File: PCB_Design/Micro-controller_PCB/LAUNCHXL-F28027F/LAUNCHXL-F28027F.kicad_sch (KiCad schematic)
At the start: 9 parts, among them CON1 USB_B_Mini, U4 TLV1117-33

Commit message: Finished Page 1 of Micro controller schematic page
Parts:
- added C10, C11: 4u7, symbol Device:C
- added C12, C13, C14, C16: 100n, symbol Device:C
- added C15: 3u3, symbol Device:C
- added C17, C18: 36p, symbol Device:C
- added D7, D8: BLUE, symbol Device:LED
- added JP1, JP2, JP3: Jumper_2_Open, symbol Jumper:Jumper_2_Open
- added L1, L2: 600 Ohm, symbol Device:FerriteBead
- added R16, R18, R19, R20, R21, R25, R28, R30, R32: 0, symbol Device:R
- added R22, R23: 1k, symbol Device:R
- added R24: 12k, symbol Device:R
- added R26, R27: 330, symbol Device:R
- added R29: 10k, symbol Device:R
- added R31: 2k2, symbol Device:R
- added U5: ISO7240MDWRG4, symbol Custom_library:ISO7240MDWRG4
- added U7: ISO7231ADW, symbol Custom_library:ISO7231ADW
- added U8: 93LC56AT-I_OT, symbol Custom_library:93LC56AT-I_OT
- added Y3: ECS-120-18-33-JEM-TR3, symbol Custom_library:ECS-120-18-33-JEM-TR3
- C9: value 0.1u -> 100n
- gave numbers to parts that had none: 1
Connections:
- net D+: now also U6.8 (DP)
- net D-: now also U6.7 (DM)
- net FTDI_3V3: now also U6.20 (VCCIO), U6.31 (VCCIO), U6.42 (VCCIO), U6.50 (VREGIN), U6.56 (VCCIO), C16.1, D7.2 (A), D8.2 (A), JP1.1 (A), L1.2, L2.2, R21.1, R22.2, R29.1, U5.1 (VCC1), U7.16 (VCC2), U8.6 (VCC)
- net GNDA: now also U6.1 (GND), U6.10 (AGND), U6.11 (GND), U6.13 (TEST), U6.15 (GND), U6.25 (GND), U6.35 (GND), U6.47 (GND), U6.5 (GND), U6.51 (GND), U6.65 (GND), C12.2, C13.2, C14.2, C15.2, C16.2, C17.2, C18.2, JP2.1 (A), R23.1, R24.2, R25.1, U5.2 (GND1_1), U5.8 (GND1_2), U7.10 (EN2), U7.15 (GND2_2), U7.9 (GND2_1), U8.2 (GND), Y3.2 (GND_1), Y3.4 (GND_2)
- net USBVCC: now also JP3.1 (A)
- net FTDI_1V8: now reaches U6.12 (VCORE)
- net FTDI_1V8: now also U6.37 (VCORE), U6.49 (VREGOUT), U6.64 (VCORE), C12.1, C13.1, C14.1, C15.1
- net ~{RESET}: now reaches U6.14 (~{RESET})
- net ~{RESET}: now also R22.1
- net at U6.16 (ADBUS0): now also R20.1, U5.3 (INA)
- net at U6.17 (ADBUS1): now also R19.1, U5.4 (INB)
- net at U6.18 (ADBUS2): now also R32.1, U7.14 (OUTA)
- net at U6.19 (ADBUS3): now also U6.38 (BDBUS0), R16.1, R18.1, U5.5 (INC), U5.6 (IND)
- net at U6.2 (OSCI): now also C17.1, Y3.1 (IN/OUT)
- net at U6.21 (ADBUS4): now also R28.1, U7.12 (INC)
- net at U6.3 (OSCO): now also C18.1, Y3.3 (OUT/IN)
- net at U6.32 (ACBUS5): now also R23.2
- net ~{SUSPEND}: now reaches U6.36 (~{SUSPEND})
- net at U6.39 (BDBUS1): now also R30.1, U7.13 (OUTB)
- net at U6.4 (VPHY): now also C10.2
- net at U6.40 (BDBUS2): now also U6.41 (BDBUS3)
- net at U6.54 (BCBUS3): now also R26.2
- net at U6.55 (BCBUS4): now also R27.2
- net REF: now reaches U6.6 (REF)
- net REF: now also R24.1
- net ~{PWREN}: now reaches U6.60 (~{PWREN})
- net FTDI_DATA: now reaches U6.61 (EEDATA)
- net FTDI_DATA: now also R31.1, U8.3 (DI)
- net FTDI_CLK: now reaches U6.62 (EECLK)
- net FTDI_CLK: now also U8.4 (CLK)
- net FTDI_CS: now reaches U6.63 (EECS)
- net FTDI_CS: now also U8.5 (CS)
- net at U6.9 (VPLL): now also C11.2
- new net: C10.1, C11.1, L1.1, L2.1
- new net: D7.1 (K), R26.1
- new net: R29.2, R31.2, U8.1 (DO)
- new net: D8.1 (K), R27.1
- new net +3.3V: JP1.2 (B), R21.2, U5.10 (EN), U5.16 (VCC2), U7.1 (VCC1)
- new net +5V: JP3.2 (B)
- new net GND: JP2.2 (B), R25.2, U5.15 (GND2_2), U5.9 (GND2_1), U7.2 (GND1_1), U7.7 (EN1), U7.8 (GND1_2)
- new net JTAG_TRST: R28.2, U7.5 (OUTC)
- new net SCI_RX: R16.2, U5.11 (OUTD)
- new net SCI_TX: R30.2, U7.4 (INB)
- new net TCK: R20.2, U5.14 (OUTA)
- new net TDI: R19.2, U5.13 (OUTB)
- new net TDO: R32.2, U7.3 (INA)
- new net TMS: R18.2, U5.12 (OUTC)
- no-connect marks 2 -> 24
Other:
- note added: "12 MHz oscillator"
- moved on the sheet: U6

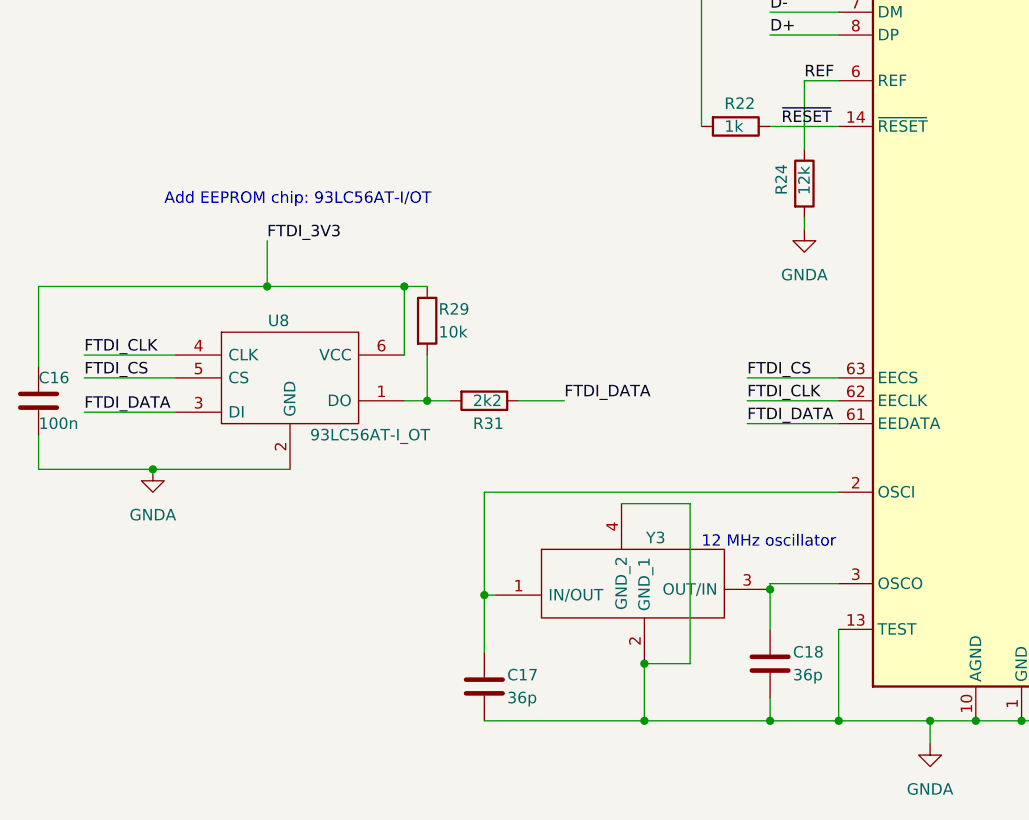
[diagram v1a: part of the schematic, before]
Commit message: IGBT Closed loop simulink model works
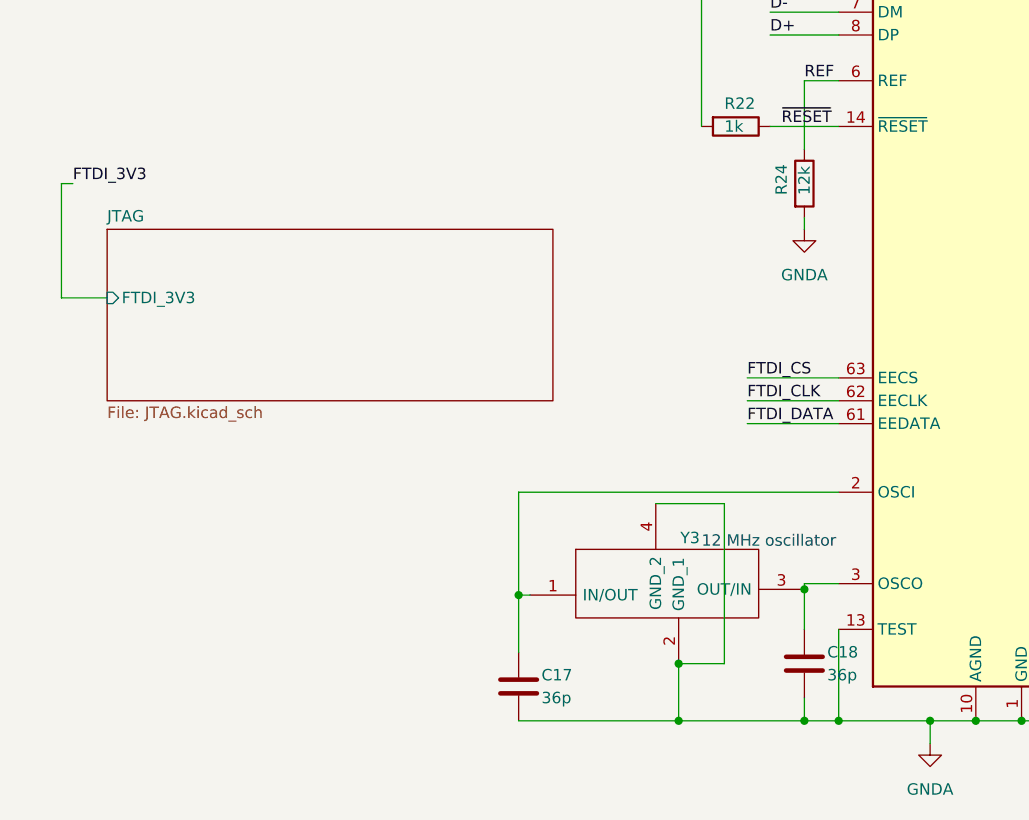
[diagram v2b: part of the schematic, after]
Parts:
- removed C16: 100n, symbol Device:C
- removed R29: 10k, symbol Device:R
- removed R31: 2k2, symbol Device:R
- removed U8: 93LC56AT-I_OT, symbol Custom_library:93LC56AT-I_OT
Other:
- added sheet JTAG (JTAG.kicad_sch)
- note removed: "Add EEPROM chip: 93LC56AT-I/OT"
- moved on the sheet: C17, C18, Y3
